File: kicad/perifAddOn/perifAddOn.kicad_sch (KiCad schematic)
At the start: 2 parts, among them J1 QTE-020-01-X-D-A, U5 AP2281-3WG-7

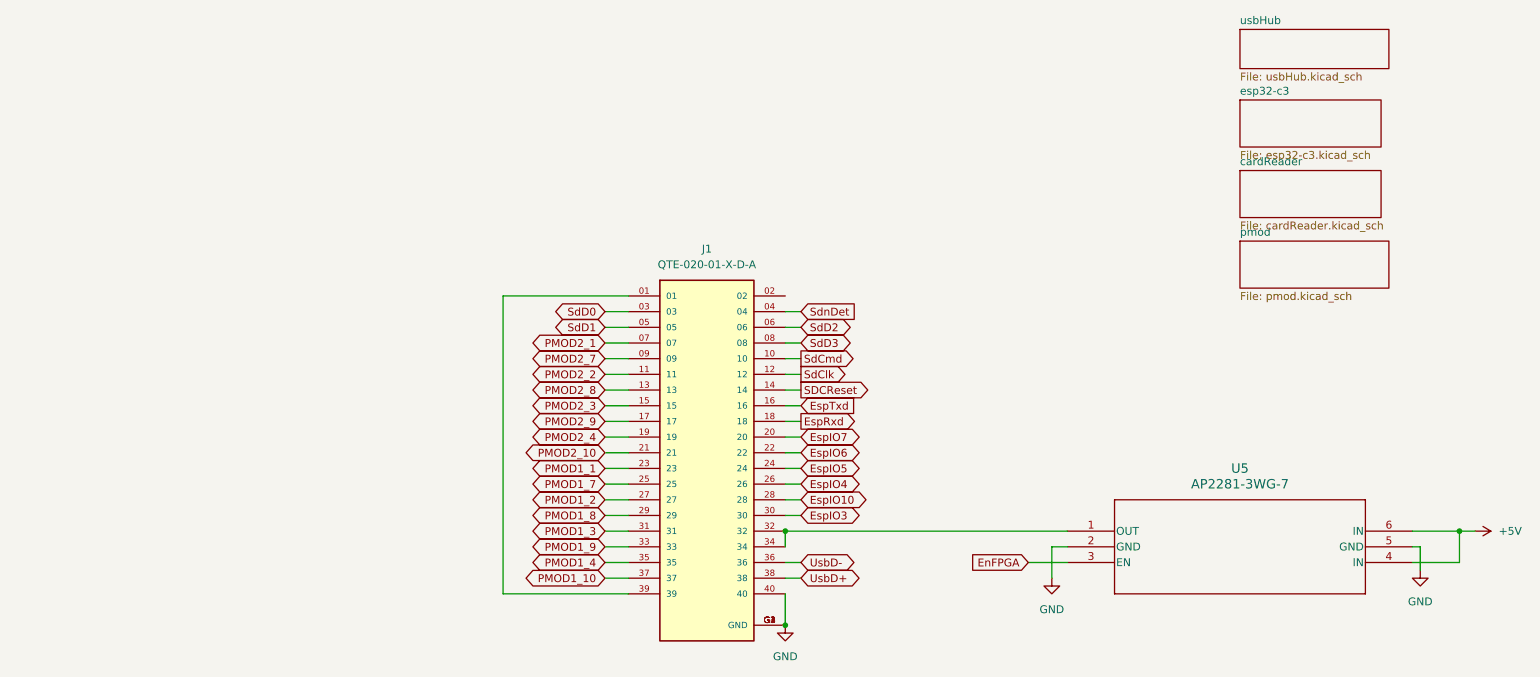
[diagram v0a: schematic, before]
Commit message: V1.1 of perifAddOn (added bus-switch on sd-card)
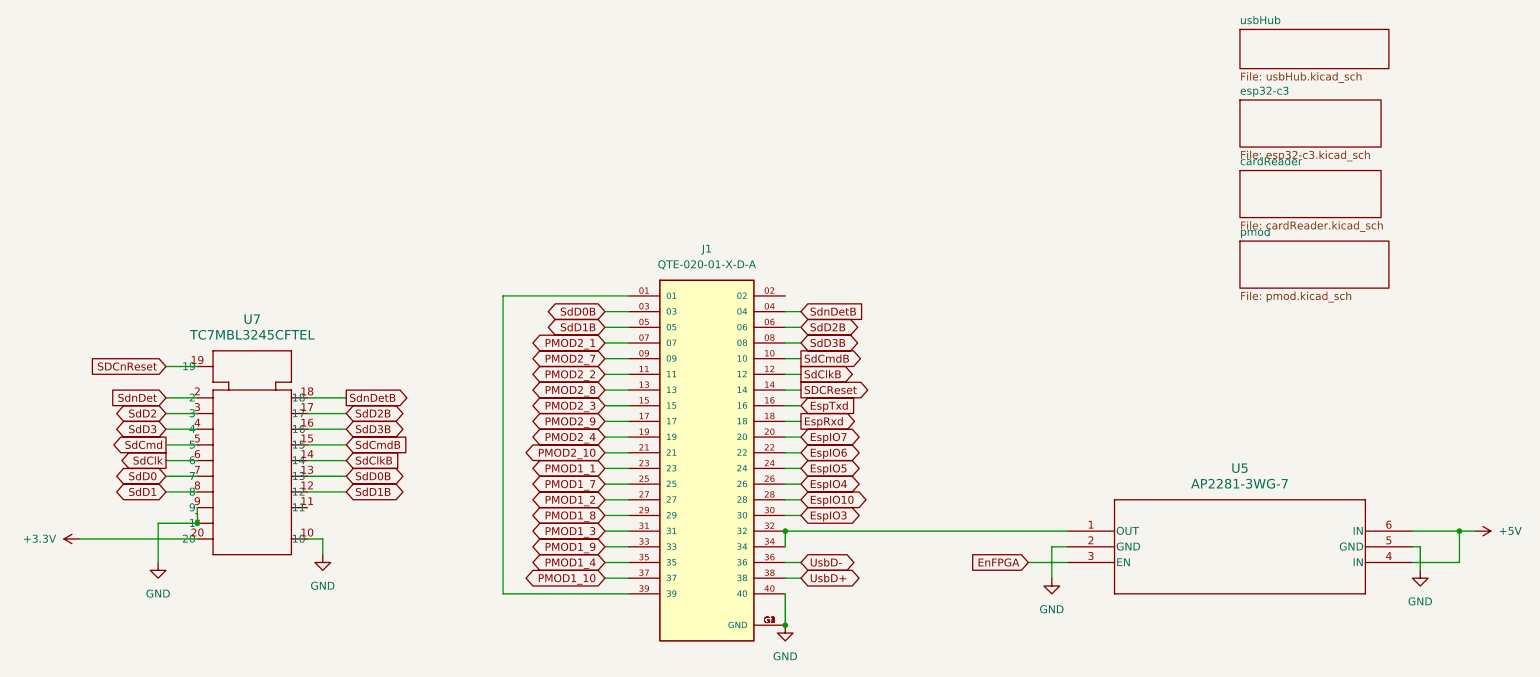
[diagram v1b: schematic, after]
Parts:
- added U7: TC7MBL3245CFTEL, addOnTemplate:TSSOP20_TOS, symbol cpuAddOn:TC7MBL3245CFTEL
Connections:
- net GND: now also U7.1, U7.10, U7.9
- net SdClk: now also U7.6; no longer J1.12
- net SdCmd: now also U7.5; no longer J1.10
- net SdD0: now also U7.7; no longer J1.03
- net SdD1: now also U7.8; no longer J1.05
- net SdD2: now also U7.3; no longer J1.06
- net SdD3: now also U7.4; no longer J1.08
- net SdnDet: now also U7.2; no longer J1.04
- new net +3.3V: U7.20
- new net SDCnReset: U7.19
- new net SdClkB: J1.12, U7.14
- new net SdCmdB: J1.10, U7.15
- new net SdD0B: J1.03, U7.13
- new net SdD1B: J1.05, U7.12
- new net SdD2B: J1.06, U7.17
- new net SdD3B: J1.08, U7.16
- new net SdnDetB: J1.04, U7.18
